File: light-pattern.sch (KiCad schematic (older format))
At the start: 27 parts

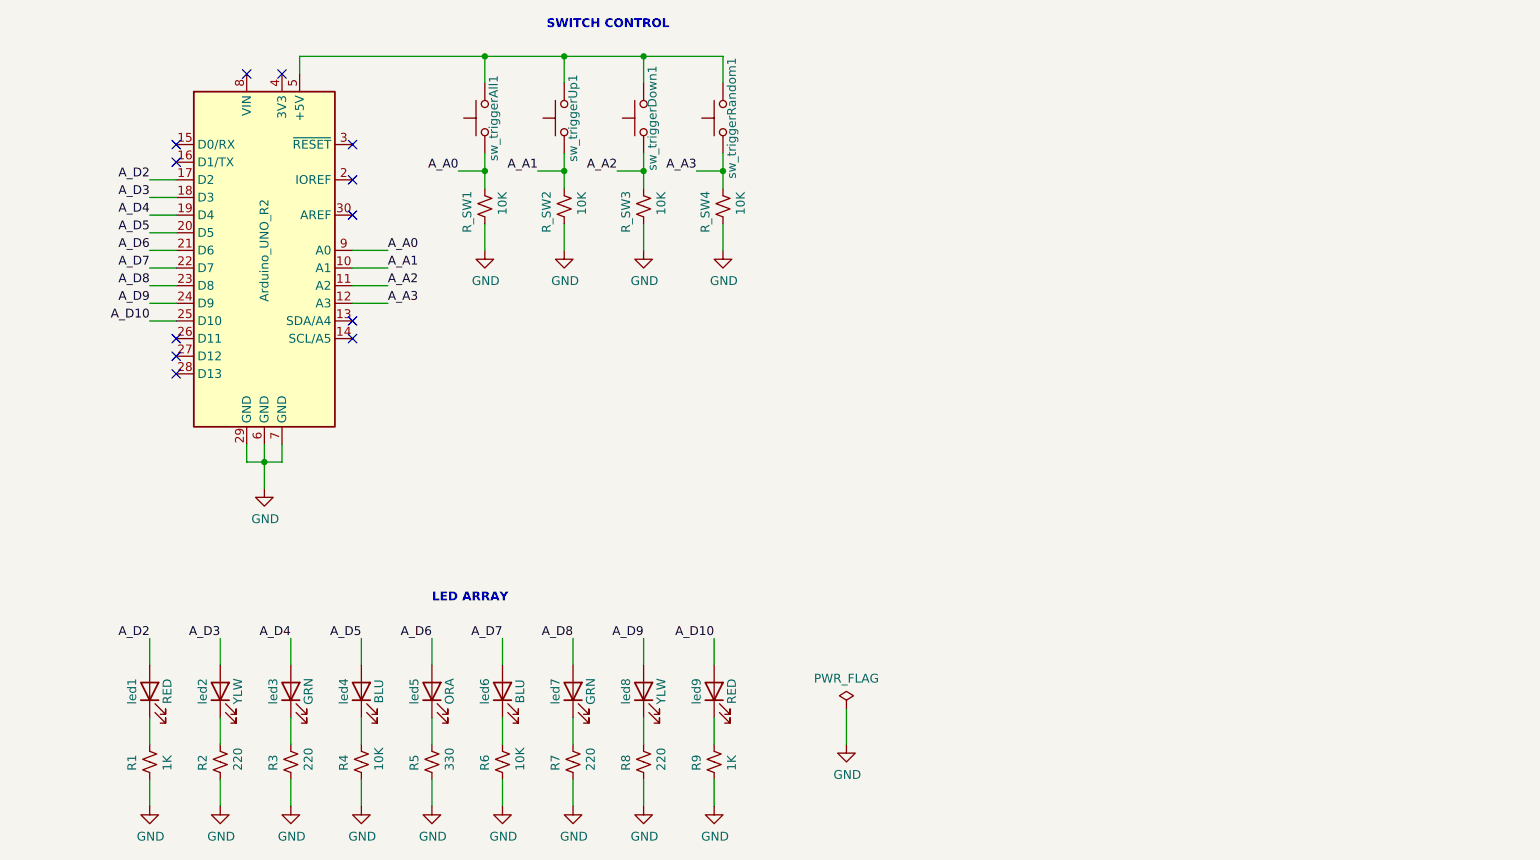
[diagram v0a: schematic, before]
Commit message: Updated uproc to Nano v3. Rewired switch control.
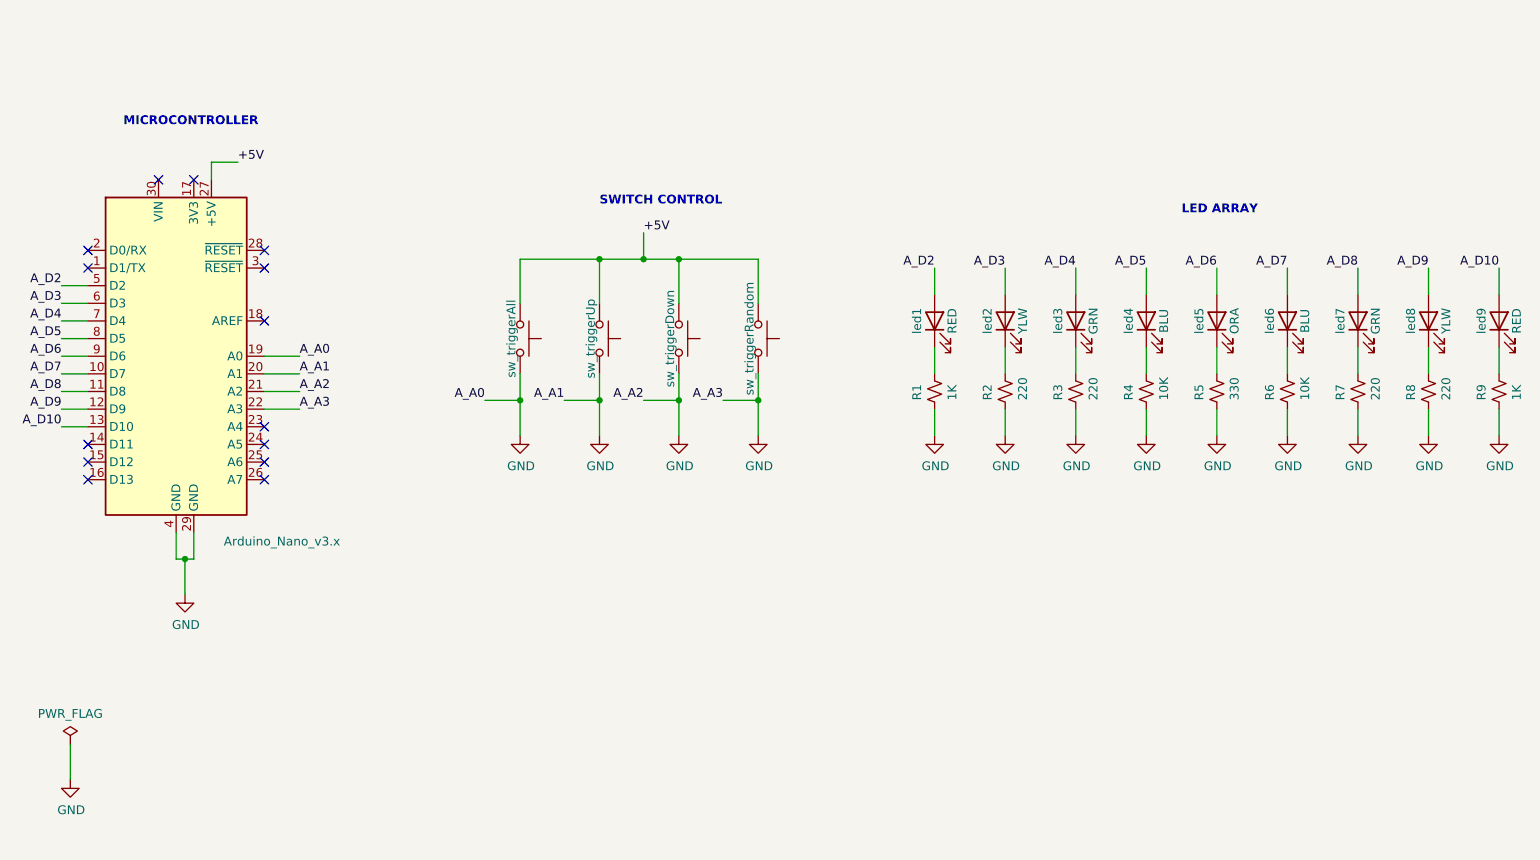
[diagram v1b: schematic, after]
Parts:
- removed Arduino_UNO_R2: Arduino_UNO_R2, Module:Arduino_UNO_R2, symbol MCU_Module:Arduino_UNO_R2
- removed R_SW1, R_SW2, R_SW3, R_SW4: 10K, Resistor_THT:R_Axial_DIN0207_L6.3mm_D2.5mm_P5.08mm_Vertical, symbol Device:R_Small_US
- removed sw_triggerDown1, sw_triggerRandom1, sw_triggerUp1: SW_Push, Button_Switch_THT:SW_PUSH_6mm, symbol Switch:SW_Push
- added A1: Arduino_Nano_v3.x, Module:Arduino_Nano, symbol MCU_Module:Arduino_Nano_v3.x
- added sw_triggerDown, sw_triggerRandom, sw_triggerUp: SW_Push, Button_Switch_THT:SW_PUSH_6mm, symbol Switch:SW_Push
- renumbered sw_triggerAll1 to sw_triggerAll
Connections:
- net A_D10: now also A1.13 (D10)
- net A_D2: now also A1.5 (D2)
- net A_D3: now also A1.6 (D3)
- net A_D4: now also A1.7 (D4)
- net A_D5: now also A1.8 (D5)
- net A_D6: now also A1.9 (D6)
- net A_D7: now also A1.10 (D7)
- net A_D8: now also A1.11 (D8)
- net A_D9: now also A1.12 (D9)
- net GND: now also sw_triggerAll.2, A1.19 (A0), A1.20 (A1), A1.21 (A2), A1.22 (A3), A1.29 (GND), A1.4 (GND), sw_triggerDown.2, sw_triggerRandom.2, sw_triggerUp.2
- net A_A0 renamed +5V
- net +5V: now also A1.27 (+5V), sw_triggerDown.1, sw_triggerRandom.1, sw_triggerUp.1
- no-connect marks 12 -> 14
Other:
- note added: "MICROCONTROLLER"
- moved on the sheet: R1, R2, R3, R4, R5, R6, R7, R8, R9, led1, led2, led3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

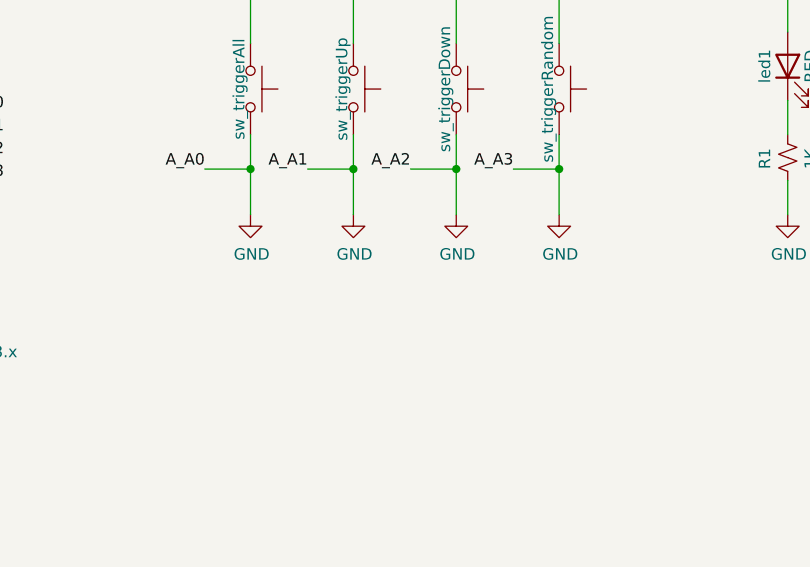
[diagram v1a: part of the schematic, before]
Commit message: Fixed bug in switch control that activates neighboring switches when pressed.
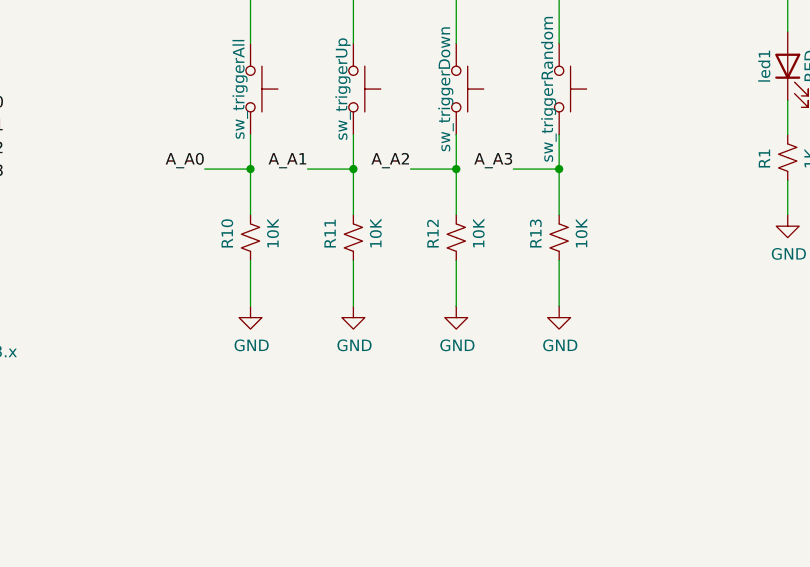
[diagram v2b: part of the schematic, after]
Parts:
- added R10, R11, R12, R13: 10K, Resistor_THT:R_Axial_DIN0207_L6.3mm_D2.5mm_P2.54mm_Vertical, symbol Device:R_Small_US
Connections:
- net GND: now also R10.2, R11.2, R12.2, R13.2; no longer A1.19 (A0), A1.20 (A1), A1.21 (A2), A1.22 (A3), sw_triggerAll.2, sw_triggerDown.2, sw_triggerRandom.2, sw_triggerUp.2
- new net A_A0: A1.19 (A0), R10.1, sw_triggerAll.2
- new net A_A1: A1.20 (A1), R11.1, sw_triggerUp.2
- new net A_A2: A1.21 (A2), R12.1, sw_triggerDown.2
- new net A_A3: A1.22 (A3), R13.1, sw_triggerRandom.2
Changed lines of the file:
@@
 L power:GND #PWR010
 U 1 1 6152A3AA
-P 3750 4250
-F 0 "#PWR010" H 3750 4000 50  0001 C CNN
-F 1 "GND" H 3755 4077 50  0000 C CNN
-F 2 "" H 3750 4250 50  0001 C CNN
-F 3 "" H 3750 4250 50  0001 C CNN
-	1    3750 4250
+P 3750 4650
+F 0 "#PWR010" H 3750 4400 50  0001 C CNN
+F 1 "GND" H 3755 4477 50  0000 C CNN
+F 2 "" H 3750 4650 50  0001 C CNN
+F 3 "" H 3750 4650 50  0001 C CNN
+	1    3750 4650
 	1    0    0    -1
 $EndComp
@@
 Wire Wire Line
 	3750 4050 3550 4050
-Connection ~ 3750 4050
-Wire Wire Line
-	3750 4050 3750 4250
+Wire Wire Line
+	3750 4450 3750 4650
 $Comp
 L Switch:SW_Push sw_triggerDown
@@
 L power:GND #PWR?
 U 1 1 617651BF
-P 4200 4250
-F 0 "#PWR?" H 4200 4000 50  0001 C CNN
-F 1 "GND" H 4205 4077 50  0000 C CNN
-F 2 "" H 4200 4250 50  0001 C CNN
-F 3 "" H 4200 4250 50  0001 C CNN
-	1    4200 4250
+P 4200 4650
+F 0 "#PWR?" H 4200 4400 50  0001 C CNN
+F 1 "GND" H 4205 4477 50  0000 C CNN
+F 2 "" H 4200 4650 50  0001 C CNN
+F 3 "" H 4200 4650 50  0001 C CNN
+	1    4200 4650
 	1    0    0    -1
 $EndComp
@@
 L power:GND #PWR?
 U 1 1 61768701
-P 4650 4250
-F 0 "#PWR?" H 4650 4000 50  0001 C CNN
-F 1 "GND" H 4655 4077 50  0000 C CNN
-F 2 "" H 4650 4250 50  0001 C CNN
-F 3 "" H 4650 4250 50  0001 C CNN
-	1    4650 4250
+P 4650 4650
+F 0 "#PWR?" H 4650 4400 50  0001 C CNN
+F 1 "GND" H 4655 4477 50  0000 C CNN
+F 2 "" H 4650 4650 50  0001 C CNN
+F 3 "" H 4650 4650 50  0001 C CNN
+	1    4650 4650
 	1    0    0    -1
 $EndComp
@@
 L power:GND #PWR?
 U 1 1 6176BA0D
-P 5100 4250
-F 0 "#PWR?" H 5100 4000 50  0001 C CNN
-F 1 "GND" H 5105 4077 50  0000 C CNN
-F 2 "" H 5100 4250 50  0001 C CNN
-F 3 "" H 5100 4250 50  0001 C CNN
-	1    5100 4250
+P 5100 4650
+F 0 "#PWR?" H 5100 4400 50  0001 C CNN
+F 1 "GND" H 5105 4477 50  0000 C CNN
+F 2 "" H 5100 4650 50  0001 C CNN
+F 3 "" H 5100 4650 50  0001 C CNN
+	1    5100 4650
 	1    0    0    -1
 $EndComp
@@
 Wire Wire Line
 	2000 2700 2150 2700
+$Comp
+L Device:R_Small_US R11
+U 1 1 61728C1E
+P 4200 4350
+F 0 "R11" V 4100 4300 50  0000 L CNN
+F 1 "10K" V 4300 4300 50  0000 L CNN
+F 2 "Resistor_THT:R_Axial_DIN0207_L6.3mm_D2.5mm_P2.54mm_Vertical" H 4200 4350 50  0001 C CNN
+F 3 "~" H 4200 4350 50  0001 C CNN
+	1    4200 4350
+	1    0    0    -1
+$EndComp
+$Comp
+L Device:R_Small_US R10
+U 1 1 6172ED45
+P 3750 4350
+F 0 "R10" V 3650 4300 50  0000 L CNN
+F 1 "10K" V 3850 4300 50  0000 L CNN
+F 2 "Resistor_THT:R_Axial_DIN0207_L6.3mm_D2.5mm_P2.54mm_Vertical" H 3750 4350 50  0001 C CNN
+F 3 "~" H 3750 4350 50  0001 C CNN
+	1    3750 4350
+	1    0    0    -1
+$EndComp
+$Comp
+L Device:R_Small_US R12
+U 1 1 6173343A
+P 4650 4350
+F 0 "R12" V 4550 4300 50  0000 L CNN
+F 1 "10K" V 4750 4300 50  0000 L CNN
+F 2 "Resistor_THT:R_Axial_DIN0207_L6.3mm_D2.5mm_P2.54mm_Vertical" H 4650 4350 50  0001 C CNN
+F 3 "~" H 4650 4350 50  0001 C CNN
+	1    4650 4350
+	1    0    0    -1
+$EndComp
+$Comp
+L Device:R_Small_US R13
+U 1 1 61733444
+P 5100 4350
+F 0 "R13" V 5000 4300 50  0000 L CNN
+F 1 "10K" V 5200 4300 50  0000 L CNN
+F 2 "Resistor_THT:R_Axial_DIN0207_L6.3mm_D2.5mm_P2.54mm_Vertical" H 5100 4350 50  0001 C CNN
+F 3 "~" H 5100 4350 50  0001 C CNN
+	1    5100 4350
+	1    0    0    -1
+$EndComp
+Wire Wire Line
+	3750 4050 3750 4250
+Connection ~ 3750 4050
+Wire Wire Line
+	4200 4450 4200 4650
+Wire Wire Line
+	4650 4450 4650 4650
+Wire Wire Line
+	5100 4450 5100 4650
 $EndSCHEMATC
